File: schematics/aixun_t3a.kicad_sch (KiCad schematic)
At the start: 90 parts, among them P3 Debug, P4 GX12-5, Q1 PNP, Q1 Q_NPN_BEC, Q3 AO4413, Q4 Q_NPN_BEC, SW1 SET, SW2 CH, U1 MY240H2416S-V2, U2 GD32F303RCT6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

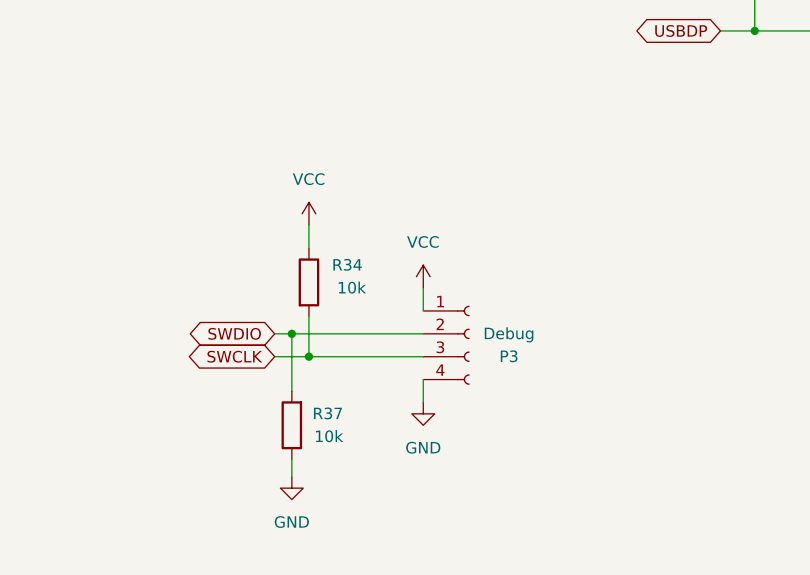
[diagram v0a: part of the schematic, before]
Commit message: schematics: Correct SWD interface
Signed-off-by: Michael Niewöhner <foss@mniewoehner.de>
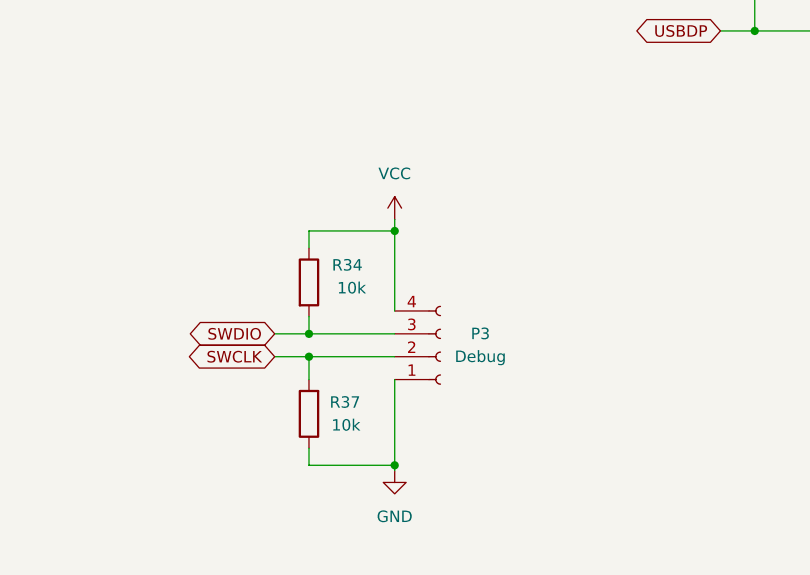
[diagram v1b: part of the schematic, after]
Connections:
- net GND: now also P3.1 (Pin_1); no longer P3.4 (Pin_4)
- net SWCLK: now also P3.2 (Pin_2), R37.2; no longer P3.3 (Pin_3), R34.2
- net SWDIO: now also P3.3 (Pin_3), R34.2; no longer P3.2 (Pin_2), R37.2
- net VCC: now also P3.4 (Pin_4); no longer P3.1 (Pin_1)
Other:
- moved on the sheet: P3, R37

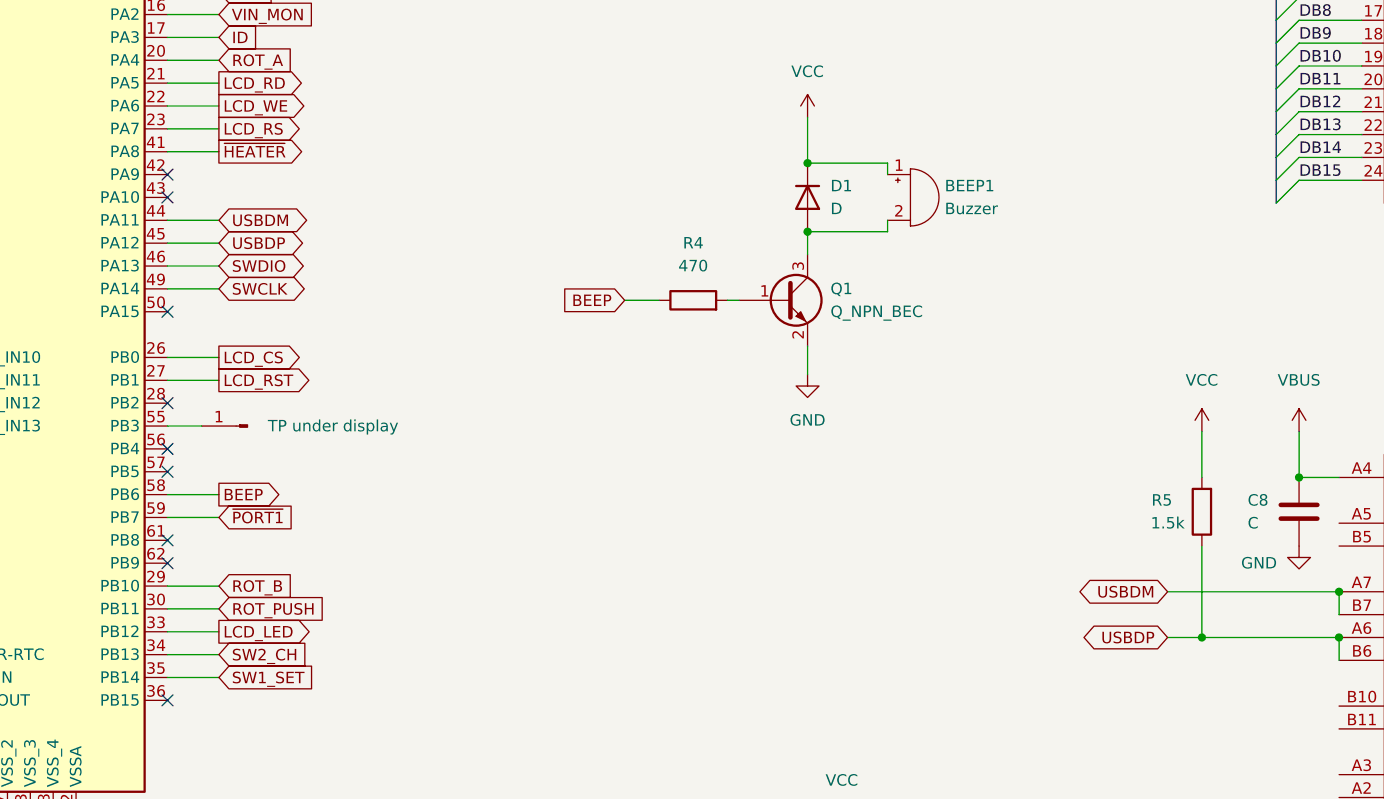
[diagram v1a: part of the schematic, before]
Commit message: schematics: Correct USB pull-up
Signed-off-by: Michael Niewöhner <foss@mniewoehner.de>
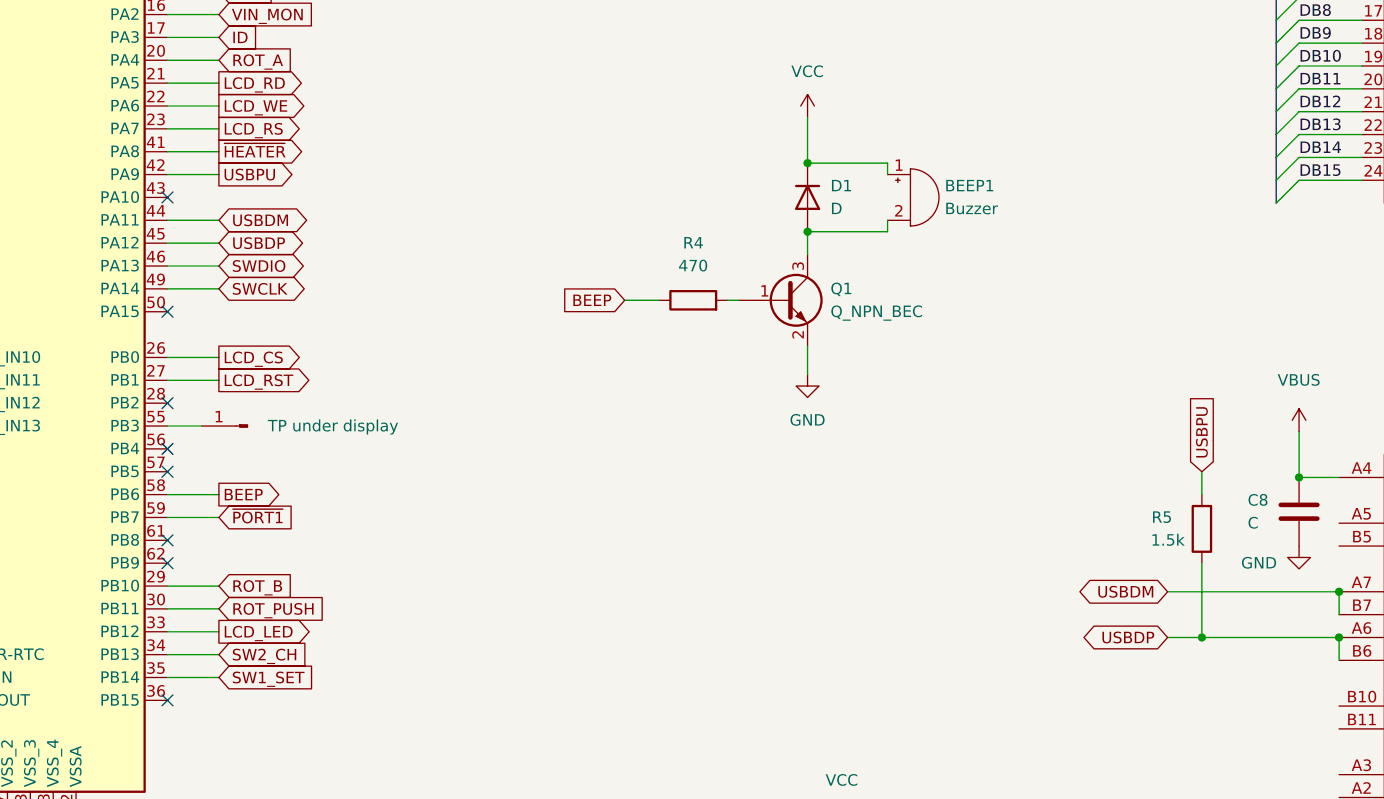
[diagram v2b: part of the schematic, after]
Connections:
- net VCC: no longer R5.2
- net USBPU: now reaches U2.42 (PA9)
- net USBPU: now also R5.2
- no-connect marks 9 -> 8
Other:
- moved on the sheet: R5
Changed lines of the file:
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@@
   (no_connect (at 102.87 196.85))
   (no_connect (at 102.87 189.23))
-  (no_connect (at 102.87 163.83))
   (no_connect (at 102.87 166.37))
   (no_connect (at 102.87 179.07))
@@
     (stroke (width 0) (type default) (color 0 0 0 0))
   )
-  (wire (pts (xy 217.805 205.105) (xy 217.805 215.265))
+  (wire (pts (xy 217.805 207.01) (xy 217.805 215.265))
     (stroke (width 0) (type default) (color 0 0 0 0))
   )
@@
     (stroke (width 0) (type default) (color 0 0 0 0))
   )
-  (wire (pts (xy 217.805 192.405) (xy 217.805 197.485))
+  (wire (pts (xy 217.805 196.85) (xy 217.805 199.39))
     (stroke (width 0) (type default) (color 0 0 0 0))
   )
@@
     (stroke (width 0) (type default) (color 0 0 0 0))
   )
+  (wire (pts (xy 102.87 163.83) (xy 108.585 163.83))
+    (stroke (width 0) (type default) (color 0 0 0 0))
+  )
   (wire (pts (xy 228.6 154.305) (xy 235.585 154.305))
     (stroke (width 0) (type default) (color 0 0 0 0))
@@
     )
   )
+  (global_label "USBPU" (shape input) (at 217.805 196.85 90) (fields_autoplaced)
+    (effects (font (size 1.27 1.27)) (justify left))
+    (property "Intersheet References" "${INTERSHEET_REFS}" (id 0) (at 217.8844 188.0264 90)
+      (effects (font (size 1.27 1.27)) (justify left) hide)
+    )
+  )
   (global_label "SWDIO" (shape bidirectional) (at 108.585 173.99 0) (fields_autoplaced)
     (effects (font (size 1.27 1.27)) (justify left))
@@
     )
   )
+  (global_label "USBPU" (shape output) (at 108.585 163.83 0) (fields_autoplaced)
+    (effects (font (size 1.27 1.27)) (justify left))
+    (property "Intersheet References" "${INTERSHEET_REFS}" (id 0) (at 117.4086 163.7506 0)
+      (effects (font (size 1.27 1.27)) (justify left) hide)
+    )
+  )
   (global_label "LCD_RD" (shape output) (at 108.585 153.67 0) (fields_autoplaced)
     (effects (font (size 1.27 1.27)) (justify left))
@@
     (pin "2")
   )
-  (symbol (lib_id "Device:R") (at 217.805 201.295 180) (unit 1)
+  (symbol (lib_id "Device:R") (at 217.805 203.2 180) (unit 1)
     (in_bom yes) (on_board yes)
-    (property "Reference" "R5" (id 0) (at 213.36 200.025 0))
-    (property "Value" "1.5k" (id 1) (at 215.9 202.565 0)
+    (property "Reference" "R5" (id 0) (at 213.36 201.93 0))
+    (property "Value" "1.5k" (id 1) (at 215.9 204.47 0)
       (effects (font (size 1.27 1.27)) (justify left))
     )
-    (property "Footprint" "" (id 2) (at 219.583 201.295 90)
+    (property "Footprint" "" (id 2) (at 219.583 203.2 90)
       (effects (font (size 1.27 1.27)) hide)
     )
-    (property "Datasheet" "~" (id 3) (at 217.805 201.295 0)
+    (property "Datasheet" "~" (id 3) (at 217.805 203.2 0)
       (effects (font (size 1.27 1.27)) hide)
     )
@@
     (pin "1")
   )
-  (symbol (lib_id "power:VCC") (at 217.805 192.405 0) (unit 1)
-    (in_bom yes) (on_board yes) (fields_autoplaced)
-    (property "Reference" "#PWR0126" (id 0) (at 217.805 196.215 0)
-      (effects (font (size 1.27 1.27)) hide)
-    )
-    (property "Value" "VCC" (id 1) (at 217.805 186.69 0))
-    (property "Footprint" "" (id 2) (at 217.805 192.405 0)
-      (effects (font (size 1.27 1.27)) hide)
-    )
-    (property "Datasheet" "" (id 3) (at 217.805 192.405 0)
-      (effects (font (size 1.27 1.27)) hide)
-    )
-    (pin "1")
-  )
   (symbol (lib_id "Device:Buzzer") (at 185.42 166.37 0) (unit 1)
     (in_bom yes) (on_board yes) (fields_autoplaced)
@@
       (reference "#PWR0125") (unit 1) (value "VBUS") (footprint "")
     )
-    (path "/f1686259-ff22-49ff-9092-7548cab5a12d"
-      (reference "#PWR0126") (unit 1) (value "VCC") (footprint "")
-    )
     (path "/886731dc-6dfe-4202-86e1-cd1501c28e7e"

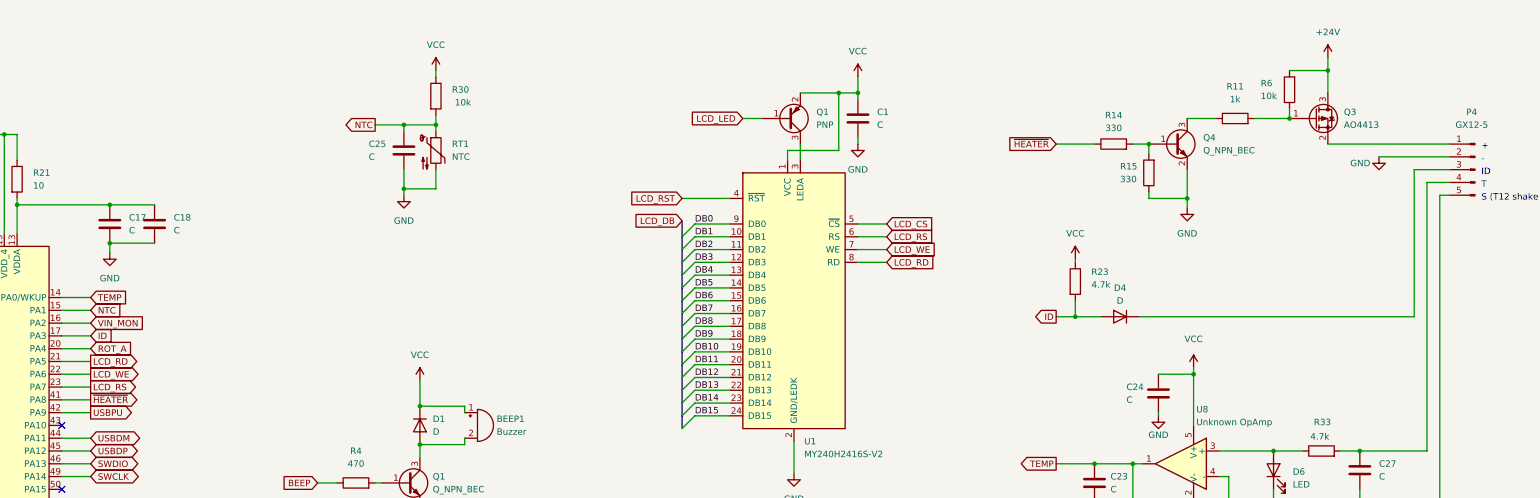
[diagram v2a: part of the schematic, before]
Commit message: schematics: Correct heater MOSFET and MCU output. Add correct symbole while at it.
Signed-off-by: Michael Niewöhner <foss@mniewoehner.de>
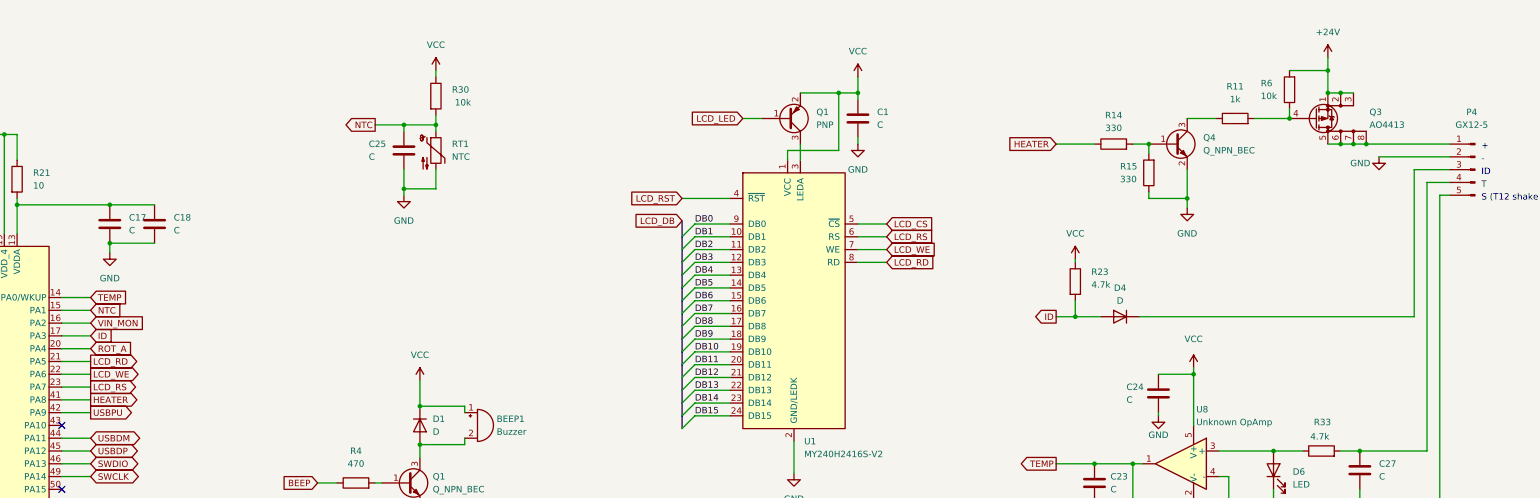
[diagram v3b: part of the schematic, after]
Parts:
- removed Q3: AO4413, symbol Device:Q_PMOS_GSD
- added Q3: AO4413, symbol AO4413:AO4413
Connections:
- net +24V: now also Q3.1 (S), Q3.2 (S), Q3.3 (S)
- net at R11.2, R6.1: now also Q3.4 (G)
- net at P4.1 (Pin_1): now also Q3.5 (D), Q3.6 (D), Q3.7 (D), Q3.8 (D)
- net ~{HEATER} renamed HEATER
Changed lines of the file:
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@@
   (junction (at 327.66 156.21) (diameter 0) (color 0 0 0 0)
   )
+  (junction (at 356.87 110.49) (diameter 0) (color 0 0 0 0)
+  )
   (junction (at 81.28 108.585) (diameter 0) (color 0 0 0 0)
   )
@@
   (junction (at 85.09 237.49) (diameter 0) (color 0 0 0 0)
   )
-  (junction (at 346.71 105.41) (diameter 0) (color 0 0 0 0)
-  )
   (junction (at 295.91 53.34) (diameter 0) (color 0 0 0 0)
   )
@@
   (junction (at 170.815 106.68) (diameter 0) (color 0 0 0 0)
   )
+  (junction (at 361.95 110.49) (diameter 0) (color 0 0 0 0)
+  )
+  (junction (at 346.71 105.41) (diameter 0) (color 0 0 0 0)
+  )
   (junction (at 37.465 158.75) (diameter 0) (color 0 0 0 0)
   )
@@
   (junction (at 354.33 95.885) (diameter 0) (color 0 0 0 0)
   )
+  (junction (at 359.41 110.49) (diameter 0) (color 0 0 0 0)
+  )
   (junction (at 86.36 108.585) (diameter 0) (color 0 0 0 0)
   )
@@
   (junction (at 334.645 182.245) (diameter 0) (color 0 0 0 0)
   )
+  (junction (at 356.87 100.33) (diameter 0) (color 0 0 0 0)
+  )
   (junction (at 276.225 48.26) (diameter 0) (color 0 0 0 0)
   )
@@
   (junction (at 217.805 56.515) (diameter 0) (color 0 0 0 0)
   )
+  (junction (at 354.33 100.33) (diameter 0) (color 0 0 0 0)
+  )
   (junction (at 360.68 171.45) (diameter 0) (color 0 0 0 0)
   )
@@
     (stroke (width 0) (type default) (color 0 0 0 0))
   )
+  (wire (pts (xy 359.41 110.49) (xy 361.95 110.49))
+    (stroke (width 0) (type default) (color 0 0 0 0))
+  )
   (bus (pts (xy 60.96 191.77) (xy 60.96 194.31))
     (stroke (width 0) (type default) (color 0 0 0 0))
@@
     (stroke (width 0) (type default) (color 0 0 0 0))
   )
-  (wire (pts (xy 354.33 110.49) (xy 378.46 110.49))
+  (wire (pts (xy 354.33 100.33) (xy 356.87 100.33))
     (stroke (width 0) (type default) (color 0 0 0 0))
   )
@@
     (stroke (width 0) (type default) (color 0 0 0 0))
   )
+  (wire (pts (xy 354.33 110.49) (xy 356.87 110.49))
+    (stroke (width 0) (type default) (color 0 0 0 0))
+  )
   (wire (pts (xy 90.17 234.95) (xy 90.17 237.49))
     (stroke (width 0) (type default) (color 0 0 0 0))
@@
     (stroke (width 0) (type default) (color 0 0 0 0))
   )
+  (wire (pts (xy 356.87 110.49) (xy 359.41 110.49))
+    (stroke (width 0) (type default) (color 0 0 0 0))
+  )
   (wire (pts (xy 168.275 239.395) (xy 168.275 237.49))
     (stroke (width 0) (type default) (color 0 0 0 0))
@@
     (stroke (width 0) (type default) (color 0 0 0 0))
   )
+  (wire (pts (xy 356.87 100.33) (xy 359.41 100.33))
+    (stroke (width 0) (type default) (color 0 0 0 0))
+  )
   (wire (pts (xy 327.66 154.94) (xy 327.66 156.21))
     (stroke (width 0) (type default) (color 0 0 0 0))
@@
     (stroke (width 0) (type default) (color 0 0 0 0))
   )
+  (wire (pts (xy 361.95 110.49) (xy 378.46 110.49))
+    (stroke (width 0) (type default) (color 0 0 0 0))
+  )
   (wire (pts (xy 346.71 103.505) (xy 346.71 105.41))
     (stroke (width 0) (type default) (color 0 0 0 0))
@@
     )
   )
-  (global_label "~{HEATER}" (shape input) (at 300.355 110.49 180) (fields_autoplaced)
+  (global_label "HEATER" (shape input) (at 300.355 110.49 180) (fields_autoplaced)
     (effects (font (size 1.27 1.27)) (justify right))
     (property "Intersheet References" "${INTERSHEET_REFS}" (id 0) (at 290.9871 110.4106 0)
@@
     )
   )
-  (global_label "~{HEATER}" (shape output) (at 108.585 161.29 0) (fields_autoplaced)
+  (global_label "HEATER" (shape output) (at 108.585 161.29 0) (fields_autoplaced)
     (effects (font (size 1.27 1.27)) (justify left))
     (property "Intersheet References" "${INTERSHEET_REFS}" (id 0) (at 117.9529 161.2106 0)
@@
     (pin "1")
   )
+  (symbol (lib_id "AO4413:AO4413") (at 351.79 105.41 0) (unit 1)
+    (in_bom yes) (on_board yes) (fields_autoplaced)
+    (property "Reference" "Q3" (id 0) (at 362.585 104.1399 0)
+      (effects (font (size 1.27 1.27)) (justify left))
+    )
+    (property "Value" "AO4413" (id 1) (at 362.585 106.6799 0)
+      (effects (font (size 1.27 1.27)) (justify left))
+    )
+    (property "Footprint" "" (id 2) (at 356.87 107.95 0)
+      (effects (font (size 1.27 1.27)) hide)
+    )
+    (property "Datasheet" "http://www.aosmd.com/pdfs/datasheet/AO4413.pdf" (id 3) (at 351.79 105.41 0)
+      (effects (font (size 1.27 1.27)) hide)
+    )
+    (pin "1")
+    (pin "2")
+    (pin "3")
+    (pin "4")
+    (pin "5")
+    (pin "6")
+    (pin "7")
+    (pin "8")
+  )
   (symbol (lib_id "Device:R") (at 268.605 37.465 0) (unit 1)
     (in_bom yes) (on_board yes)
@@
     (pin "2")
   )
-  (symbol (lib_id "Device:Q_PMOS_GSD") (at 351.79 105.41 0) (unit 1)
-    (in_bom yes) (on_board yes) (fields_autoplaced)
-    (property "Reference" "Q3" (id 0) (at 357.505 104.1399 0)
-      (effects (font (size 1.27 1.27)) (justify left))
-    )
-    (property "Value" "AO4413" (id 1) (at 357.505 106.6799 0)
-      (effects (font (size 1.27 1.27)) (justify left))
-    )
-    (property "Footprint" "" (id 2) (at 356.87 102.87 0)
-      (effects (font (size 1.27 1.27)) hide)
-    )
-    (property "Datasheet" "~" (id 3) (at 351.79 105.41 0)
-      (effects (font (size 1.27 1.27)) hide)
-    )
-    (pin "1")
-    (pin "2")
-    (pin "3")
-  )
   (symbol (lib_id "power:GND") (at 112.395 132.08 0) (unit 1)
     (in_bom yes) (on_board yes) (fields_autoplaced)
@@
       (reference "Q1") (unit 1) (value "PNP") (footprint "")
     )
-    (path "/82420d5c-1db9-4cbb-970c-ed6d53ecbe50"
+    (path "/43b4759c-7d17-46b2-a4b4-a692c8d2affc"
       (reference "Q3") (unit 1) (value "AO4413") (footprint "")
     )

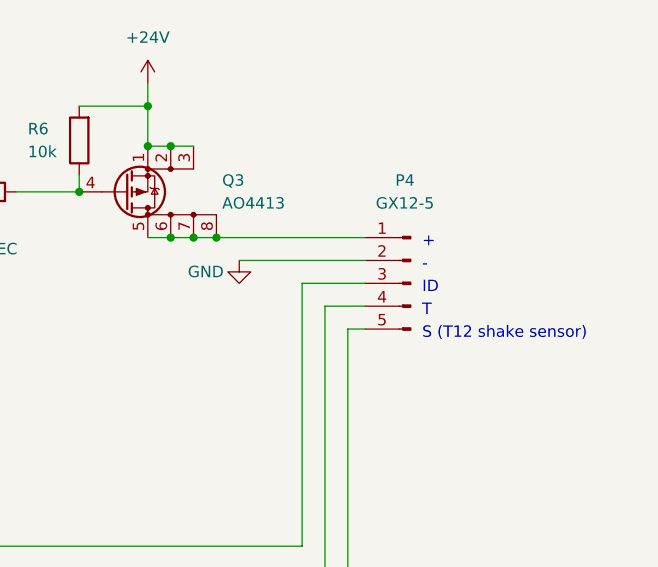
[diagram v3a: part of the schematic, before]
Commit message: schematics: Correct connector numbering
Signed-off-by: Michael Niewöhner <foss@mniewoehner.de>
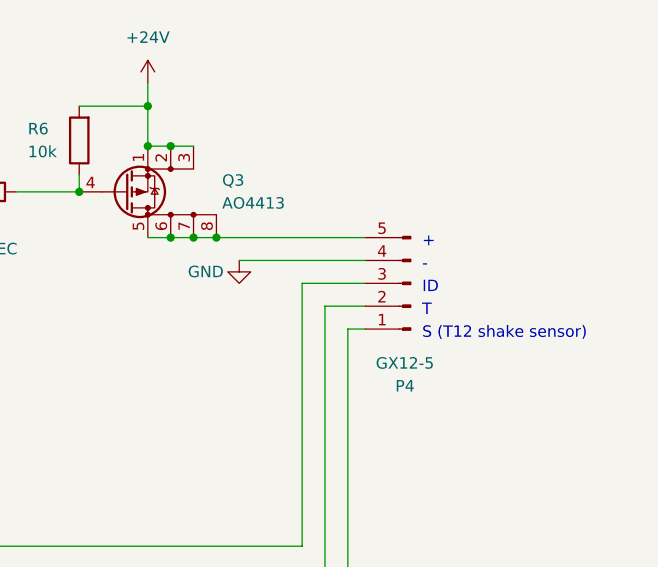
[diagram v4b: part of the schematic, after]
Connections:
- net GND: now also P4.4 (Pin_4); no longer P4.2 (Pin_2)
- net at D3.1 (K): now also P4.1 (Pin_1); no longer P4.5 (Pin_5)
- net at Q3.5 (D), Q3.6 (D), Q3.7 (D)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: now also P4.5 (Pin_5); no longer P4.1 (Pin_1)
- net at C27.1, R33.2: now also P4.2 (Pin_2); no longer P4.4 (Pin_4)
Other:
- moved on the sheet: P4
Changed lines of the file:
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@@
     (pin "2")
   )
-  (symbol (lib_id "Connector:Conn_01x05_Male") (at 383.54 115.57 0) (mirror y) (unit 1)
+  (symbol (lib_id "Connector:Conn_01x05_Male") (at 383.54 115.57 180) (unit 1)
     (in_bom yes) (on_board yes)
-    (property "Reference" "P4" (id 0) (at 382.905 104.14 0))
-    (property "Value" "GX12-5" (id 1) (at 382.905 106.68 0))
+    (property "Reference" "P4" (id 0) (at 382.905 127 0))
+    (property "Value" "GX12-5" (id 1) (at 382.905 124.46 0))
     (property "Footprint" "" (id 2) (at 383.54 115.57 0)
       (effects (font (size 1.27 1.27)) hide)
